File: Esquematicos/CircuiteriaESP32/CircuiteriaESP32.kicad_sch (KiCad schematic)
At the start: 8 parts, among them J1 Conn_01x19, J2 Conn_01x19

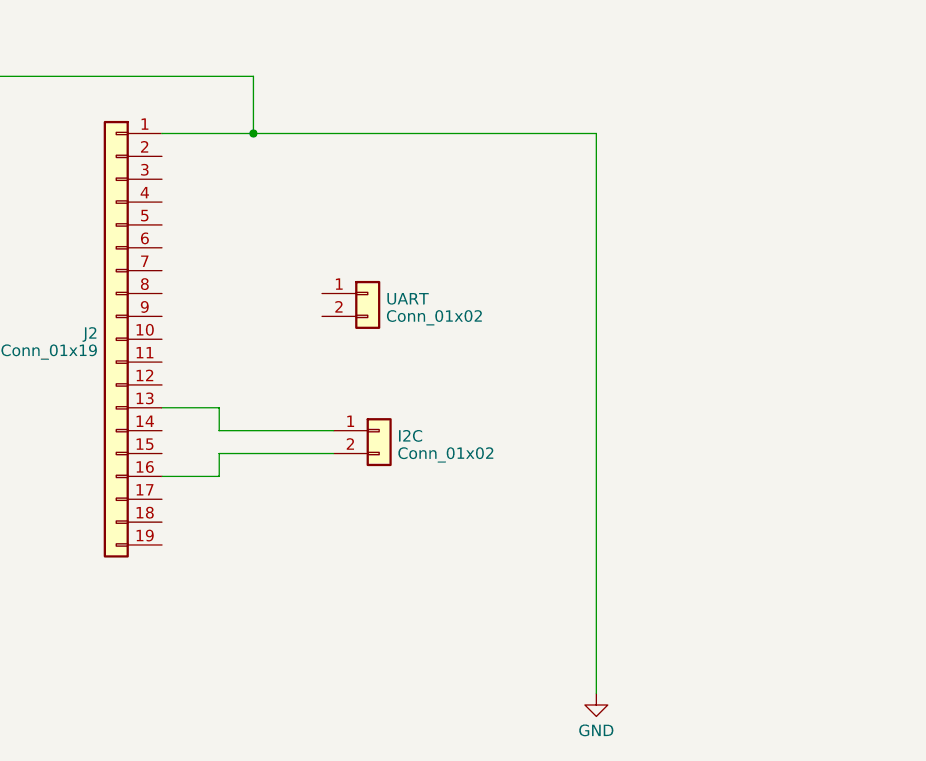
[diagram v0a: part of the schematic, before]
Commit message: Mejoras en el disenio kicad y más código generado
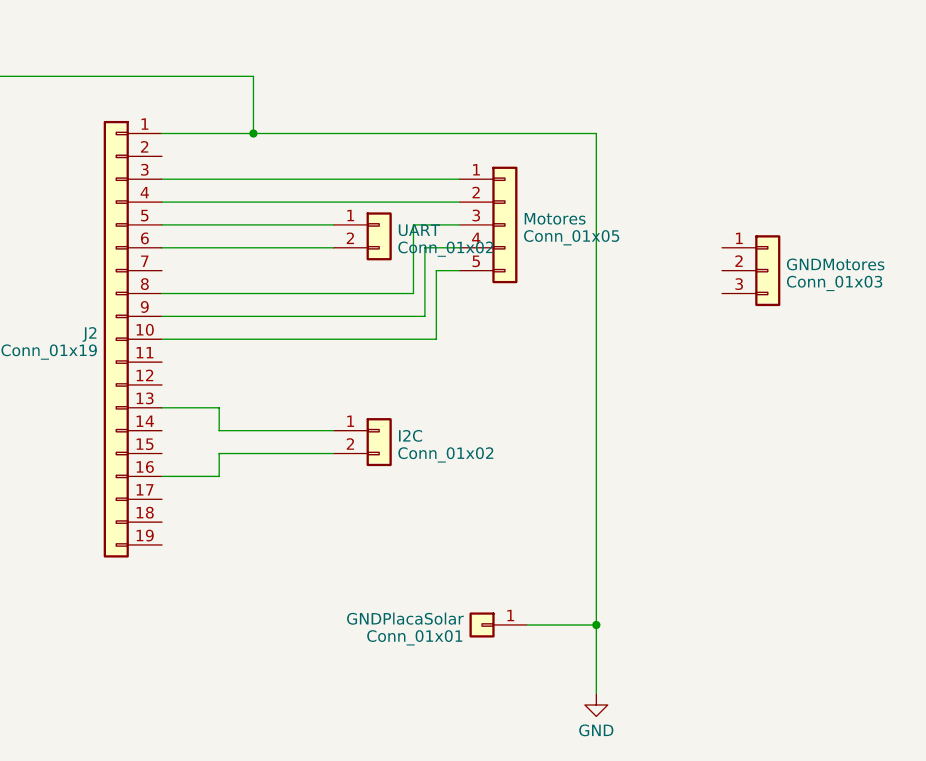
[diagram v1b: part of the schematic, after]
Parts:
- added GNDMotores: Conn_01x03, symbol Connector_Generic:Conn_01x03
- added GNDPlacaSolar: Conn_01x01, symbol Connector_Generic:Conn_01x01
- added Motores: Conn_01x05, symbol Connector_Generic:Conn_01x05
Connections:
- net GND: now also GNDPlacaSolar.1 (Pin_1)
- net at J2.10 (Pin_10): now also Motores.5 (Pin_5)
- net at J2.3 (Pin_3): now also Motores.1 (Pin_1)
- net at J2.4 (Pin_4): now also Motores.2 (Pin_2)
- net at J2.5 (Pin_5): now also UART.1 (Pin_1)
- net at J2.6 (Pin_6): now also UART.2 (Pin_2)
- net at J2.8 (Pin_8): now also Motores.3 (Pin_3)
- net at J2.9 (Pin_9): now also Motores.4 (Pin_4)
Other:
- moved on the sheet: UART
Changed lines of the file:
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@@
   (junction (at 86.36 45.72) (diameter 0) (color 0 0 0 0)
   )
+  (junction (at 184.15 100.33) (diameter 0) (color 0 0 0 0)
+  )
   (junction (at 64.77 45.72) (diameter 0) (color 0 0 0 0)
   )
@@
   (junction (at 90.17 63.5) (diameter 0) (color 0 0 0 0)
   )
+  (wire (pts (xy 168.91 60.96) (xy 166.37 60.96))
+    (stroke (width 0) (type default))
+  )
   (wire (pts (xy 64.77 91.44) (xy 64.77 76.2))
     (stroke (width 0) (type default))
@@
     (stroke (width 0) (type default))
   )
+  (wire (pts (xy 135.89 58.42) (xy 154.94 58.42))
+    (stroke (width 0) (type default))
+  )
   (wire (pts (xy 101.6 39.37) (xy 86.36 39.37))
     (stroke (width 0) (type default))
   )
+  (wire (pts (xy 163.83 63.5) (xy 135.89 63.5))
+    (stroke (width 0) (type default))
+  )
   (wire (pts (xy 64.77 76.2) (xy 69.85 76.2))
     (stroke (width 0) (type default))
   )
+  (wire (pts (xy 168.91 55.88) (xy 163.83 55.88))
+    (stroke (width 0) (type default))
+  )
+  (wire (pts (xy 176.53 100.33) (xy 184.15 100.33))
+    (stroke (width 0) (type default))
+  )
+  (wire (pts (xy 135.89 50.8) (xy 168.91 50.8))
+    (stroke (width 0) (type default))
+  )
   (wire (pts (xy 90.17 63.5) (xy 88.9 63.5))
     (stroke (width 0) (type default))
@@
     (stroke (width 0) (type default))
   )
+  (wire (pts (xy 168.91 58.42) (xy 165.1 58.42))
+    (stroke (width 0) (type default))
+  )
   (wire (pts (xy 135.89 45.72) (xy 146.05 45.72))
     (stroke (width 0) (type default))
@@
     (stroke (width 0) (type default))
   )
+  (wire (pts (xy 165.1 58.42) (xy 165.1 66.04))
+    (stroke (width 0) (type default))
+  )
   (wire (pts (xy 92.71 91.44) (xy 64.77 91.44))
     (stroke (width 0) (type default))
@@
     (stroke (width 0) (type default))
   )
-  (wire (pts (xy 184.15 45.72) (xy 184.15 107.95))
+  (wire (pts (xy 184.15 45.72) (xy 184.15 100.33))
+    (stroke (width 0) (type default))
+  )
+  (wire (pts (xy 166.37 60.96) (xy 166.37 68.58))
     (stroke (width 0) (type default))
   )
@@
     (stroke (width 0) (type default))
   )
+  (wire (pts (xy 166.37 68.58) (xy 135.89 68.58))
+    (stroke (width 0) (type default))
+  )
+  (wire (pts (xy 135.89 55.88) (xy 154.94 55.88))
+    (stroke (width 0) (type default))
+  )
   (wire (pts (xy 154.94 81.28) (xy 142.24 81.28))
     (stroke (width 0) (type default))
@@
   )
   (wire (pts (xy 88.9 58.42) (xy 92.71 58.42))
+    (stroke (width 0) (type default))
+  )
+  (wire (pts (xy 135.89 53.34) (xy 168.91 53.34))
+    (stroke (width 0) (type default))
+  )
+  (wire (pts (xy 165.1 66.04) (xy 135.89 66.04))
+    (stroke (width 0) (type default))
+  )
+  (wire (pts (xy 184.15 100.33) (xy 184.15 107.95))
+    (stroke (width 0) (type default))
+  )
+  (wire (pts (xy 163.83 55.88) (xy 163.83 63.5))
     (stroke (width 0) (type default))
   )
@@
     )
   )
+  (symbol (lib_id "Connector_Generic:Conn_01x03") (at 203.2 60.96 0) (unit 1)
+    (in_bom yes) (on_board yes) (dnp no) (fields_autoplaced)
+    (property "Reference" "GNDMotores" (at 205.232 60.3163 0)
+      (effects (font (size 1.27 1.27)) (justify left))
+    )
+    (property "Value" "Conn_01x03" (at 205.232 62.2373 0)
+      (effects (font (size 1.27 1.27)) (justify left))
+    )
+    (property "Footprint" "" (at 203.2 60.96 0)
+      (effects (font (size 1.27 1.27)) hide)
+    )
+    (property "Datasheet" "~" (at 203.2 60.96 0)
+      (effects (font (size 1.27 1.27)) hide)
+    )
+    (pin "1")
+    (pin "2")
+    (pin "3")
+    (instances
+      (project "CircuiteriaESP32"
+        (path "/916eeabf-7d1d-4f94-90a9-b50ef7656e3c"
+          (reference "GNDMotores") (unit 1)
+        )
+      )
+    )
+  )
   (symbol (lib_id "Device:C_Polarized_US") (at 105.41 39.37 90) (unit 1)
     (in_bom yes) (on_board yes) (dnp no) (fields_autoplaced)
@@
         (path "/916eeabf-7d1d-4f94-90a9-b50ef7656e3c"
           (reference "C1") (unit 1)
+        )
+      )
+    )
+  )
+  (symbol (lib_id "Connector_Generic:Conn_01x05") (at 173.99 55.88 0) (unit 1)
+    (in_bom yes) (on_board yes) (dnp no) (fields_autoplaced)
+    (property "Reference" "Motores" (at 176.022 55.2363 0)
+      (effects (font (size 1.27 1.27)) (justify left))
+    )
+    (property "Value" "Conn_01x05" (at 176.022 57.1573 0)
+      (effects (font (size 1.27 1.27)) (justify left))
+    )
+    (property "Footprint" "" (at 173.99 55.88 0)
+      (effects (font (size 1.27 1.27)) hide)
+    )
+    (property "Datasheet" "~" (at 173.99 55.88 0)
+      (effects (font (size 1.27 1.27)) hide)
+    )
+    (pin "1")
+    (pin "2")
+    (pin "3")
+    (pin "4")
+    (pin "5")
+    (instances
+      (project "CircuiteriaESP32"
+        (path "/916eeabf-7d1d-4f94-90a9-b50ef7656e3c"
+          (reference "Motores") (unit 1)
         )
       )
@@
     )
   )
-  (symbol (lib_id "Connector_Generic:Conn_01x02") (at 158.75 63.5 0) (unit 1)
-    (in_bom yes) (on_board yes) (dnp no) (fields_autoplaced)
-    (property "Reference" "UART" (at 160.782 64.1263 0)
-      (effects (font (size 1.27 1.27)) (justify left))
-    )
-    (property "Value" "Conn_01x02" (at 160.782 66.0473 0)
-      (effects (font (size 1.27 1.27)) (justify left))
-    )
-    (property "Footprint" "" (at 158.75 63.5 0)
-      (effects (font (size 1.27 1.27)) hide)
-    )
-    (property "Datasheet" "~" (at 158.75 63.5 0)
+  (symbol (lib_id "Connector_Generic:Conn_01x02") (at 160.02 55.88 0) (unit 1)
+    (in_bom yes) (on_board yes) (dnp no) (fields_autoplaced)
+    (property "Reference" "UART" (at 162.052 56.5063 0)
+      (effects (font (size 1.27 1.27)) (justify left))
+    )
+    (property "Value" "Conn_01x02" (at 162.052 58.4273 0)
+      (effects (font (size 1.27 1.27)) (justify left))
+    )
+    (property "Footprint" "" (at 160.02 55.88 0)
+      (effects (font (size 1.27 1.27)) hide)
+    )
+    (property "Datasheet" "~" (at 160.02 55.88 0)
       (effects (font (size 1.27 1.27)) hide)
     )
@@
         )
       )
+    )
+  )
+  (symbol (lib_id "Connector_Generic:Conn_01x01") (at 171.45 100.33 0) (mirror y) (unit 1)
+    (in_bom yes) (on_board yes) (dnp no)
+    (property "Reference" "GNDPlacaSolar" (at 169.418 99.6863 0)
+      (effects (font (size 1.27 1.27)) (justify left))
+    )
+    (property "Value" "Conn_01x01" (at 169.418 101.6073 0)
+      (effects (font (size 1.27 1.27)) (justify left))
+    )
+    (property "Footprint" "" (at 171.45 100.33 0)
+      (effects (font (size 1.27 1.27)) hide)
+    )
+    (property "Datasheet" "~" (at 171.45 100.33 0)
+      (effects (font (size 1.27 1.27)) hide)
+    )
+    (pin "1")
+    (instances
+      (project "CircuiteriaESP32"
+        (path "/916eeabf-7d1d-4f94-90a9-b50ef7656e3c"
+          (reference "GNDPlacaSolar") (unit 1)
+        )
+      )

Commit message: Ajustadas algunas cosas, to-do
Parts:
- added GPSRX: Conn_01x01, symbol Connector_Generic:Conn_01x01
- added R1, R2: 4k7, symbol Device:R
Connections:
- net +5V: now also R1.2, R2.2
- net at I2C.1 (Pin_1), J2.13 (Pin_13): now also R2.1
- net at I2C.2 (Pin_2), J2.16 (Pin_16): now also R1.1
- net at Motores.1 (Pin_1): now also J2.2 (Pin_2); no longer J2.3 (Pin_3)
- net at Motores.2 (Pin_2): now also J2.3 (Pin_3); no longer J2.4 (Pin_4)
- net at Motores.3 (Pin_3): now also J2.6 (Pin_6); no longer J2.8 (Pin_8)
- net at Motores.4 (Pin_4): now also J2.8 (Pin_8); no longer J2.9 (Pin_9)
- net at J2.10 (Pin_10): now also GPSRX.1 (Pin_1); no longer Motores.5 (Pin_5)
- net at UART.1 (Pin_1): now also J2.4 (Pin_4); no longer J2.5 (Pin_5)
- net at UART.2 (Pin_2): now also J2.5 (Pin_5); no longer J2.6 (Pin_6)
- new net: J2.9 (Pin_9), Motores.5 (Pin_5)
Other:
- moved on the sheet: UART
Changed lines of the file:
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@@
 (kicad_sch (version 20230121) (generator eeschema)
   (paper "A4")
+  (junction (at 146.05 97.79) (diameter 0) (color 0 0 0 0)
+  )
+  (junction (at 146.05 81.28) (diameter 0) (color 0 0 0 0)
+  )
   (junction (at 64.77 76.2) (diameter 0) (color 0 0 0 0)
   )
   (junction (at 86.36 45.72) (diameter 0) (color 0 0 0 0)
   )
+  (junction (at 153.67 78.74) (diameter 0) (color 0 0 0 0)
+  )
   (junction (at 184.15 100.33) (diameter 0) (color 0 0 0 0)
   )
@@
   (junction (at 90.17 63.5) (diameter 0) (color 0 0 0 0)
   )
-  (wire (pts (xy 168.91 60.96) (xy 166.37 60.96))
-    (stroke (width 0) (type default))
+  (junction (at 64.77 91.44) (diameter 0) (color 0 0 0 0)
   )
   (wire (pts (xy 64.77 91.44) (xy 64.77 76.2))
@@
     (stroke (width 0) (type default))
   )
-  (wire (pts (xy 135.89 58.42) (xy 154.94 58.42))
+  (wire (pts (xy 165.1 58.42) (xy 165.1 63.5))
+    (stroke (width 0) (type default))
+  )
+  (wire (pts (xy 153.67 78.74) (xy 142.24 78.74))
+    (stroke (width 0) (type default))
+  )
+  (wire (pts (xy 146.05 92.71) (xy 146.05 97.79))
     (stroke (width 0) (type default))
   )
@@
     (stroke (width 0) (type default))
   )
-  (wire (pts (xy 163.83 63.5) (xy 135.89 63.5))
-    (stroke (width 0) (type default))
-  )
   (wire (pts (xy 64.77 76.2) (xy 69.85 76.2))
     (stroke (width 0) (type default))
   )
-  (wire (pts (xy 168.91 55.88) (xy 163.83 55.88))
+  (wire (pts (xy 135.89 66.04) (xy 167.64 66.04))
     (stroke (width 0) (type default))
   )
@@
     (stroke (width 0) (type default))
   )
-  (wire (pts (xy 135.89 50.8) (xy 168.91 50.8))
-    (stroke (width 0) (type default))
-  )
   (wire (pts (xy 90.17 63.5) (xy 88.9 63.5))
     (stroke (width 0) (type default))
   )
+  (wire (pts (xy 135.89 55.88) (xy 154.94 55.88))
+    (stroke (width 0) (type default))
+  )
+  (wire (pts (xy 176.53 74.93) (xy 153.67 74.93))
+    (stroke (width 0) (type default))
+  )
   (wire (pts (xy 86.36 45.72) (xy 92.71 45.72))
     (stroke (width 0) (type default))
@@
     (stroke (width 0) (type default))
   )
+  (wire (pts (xy 162.56 58.42) (xy 135.89 58.42))
+    (stroke (width 0) (type default))
+  )
+  (wire (pts (xy 168.91 58.42) (xy 165.1 58.42))
+    (stroke (width 0) (type default))
+  )
+  (wire (pts (xy 153.67 85.09) (xy 176.53 85.09))
+    (stroke (width 0) (type default))
+  )
   (wire (pts (xy 64.77 76.2) (xy 64.77 45.72))
     (stroke (width 0) (type default))
   )
-  (wire (pts (xy 168.91 58.42) (xy 165.1 58.42))
-    (stroke (width 0) (type default))
-  )
   (wire (pts (xy 135.89 45.72) (xy 146.05 45.72))
     (stroke (width 0) (type default))
@@
     (stroke (width 0) (type default))
   )
+  (wire (pts (xy 168.91 53.34) (xy 166.37 53.34))
+    (stroke (width 0) (type default))
+  )
   (wire (pts (xy 88.9 63.5) (xy 88.9 64.77))
     (stroke (width 0) (type default))
   )
-  (wire (pts (xy 165.1 58.42) (xy 165.1 66.04))
+  (wire (pts (xy 135.89 53.34) (xy 154.94 53.34))
+    (stroke (width 0) (type default))
+  )
+  (wire (pts (xy 176.53 85.09) (xy 176.53 74.93))
     (stroke (width 0) (type default))
   )
@@
     (stroke (width 0) (type default))
   )
-  (wire (pts (xy 166.37 60.96) (xy 166.37 68.58))
+  (wire (pts (xy 168.91 50.8) (xy 167.64 50.8))
     (stroke (width 0) (type default))
   )
@@
     (stroke (width 0) (type default))
   )
-  (wire (pts (xy 166.37 68.58) (xy 135.89 68.58))
-    (stroke (width 0) (type default))
-  )
-  (wire (pts (xy 135.89 55.88) (xy 154.94 55.88))
-    (stroke (width 0) (type default))
-  )
-  (wire (pts (xy 154.94 81.28) (xy 142.24 81.28))
+  (wire (pts (xy 154.94 81.28) (xy 146.05 81.28))
     (stroke (width 0) (type default))
   )
@@
     (stroke (width 0) (type default))
   )
+  (wire (pts (xy 167.64 60.96) (xy 167.64 66.04))
+    (stroke (width 0) (type default))
+  )
+  (wire (pts (xy 146.05 97.79) (xy 64.77 97.79))
+    (stroke (width 0) (type default))
+  )
   (wire (pts (xy 90.17 76.2) (xy 90.17 63.5))
     (stroke (width 0) (type default))
   )
-  (wire (pts (xy 154.94 78.74) (xy 142.24 78.74))
+  (wire (pts (xy 154.94 78.74) (xy 153.67 78.74))
     (stroke (width 0) (type default))
   )
@@
     (stroke (width 0) (type default))
   )
+  (wire (pts (xy 167.64 50.8) (xy 167.64 48.26))
+    (stroke (width 0) (type default))
+  )
+  (wire (pts (xy 162.56 55.88) (xy 162.56 58.42))
+    (stroke (width 0) (type default))
+  )
   (wire (pts (xy 64.77 41.91) (xy 64.77 45.72))
     (stroke (width 0) (type default))
   )
+  (wire (pts (xy 146.05 81.28) (xy 146.05 85.09))
+    (stroke (width 0) (type default))
+  )
   (wire (pts (xy 146.05 39.37) (xy 146.05 45.72))
     (stroke (width 0) (type default))
   )
+  (wire (pts (xy 146.05 81.28) (xy 142.24 81.28))
+    (stroke (width 0) (type default))
+  )
+  (wire (pts (xy 153.67 74.93) (xy 153.67 78.74))
+    (stroke (width 0) (type default))
+  )
+  (wire (pts (xy 168.91 60.96) (xy 167.64 60.96))
+    (stroke (width 0) (type default))
+  )
+  (wire (pts (xy 153.67 92.71) (xy 153.67 97.79))
+    (stroke (width 0) (type default))
+  )
   (wire (pts (xy 146.05 45.72) (xy 184.15 45.72))
     (stroke (width 0) (type default))
@@
     (stroke (width 0) (type default))
   )
-  (wire (pts (xy 135.89 53.34) (xy 168.91 53.34))
-    (stroke (width 0) (type default))
-  )
-  (wire (pts (xy 165.1 66.04) (xy 135.89 66.04))
+  (wire (pts (xy 153.67 97.79) (xy 146.05 97.79))
+    (stroke (width 0) (type default))
+  )
+  (wire (pts (xy 166.37 53.34) (xy 166.37 50.8))
+    (stroke (width 0) (type default))
+  )
+  (wire (pts (xy 167.64 48.26) (xy 135.89 48.26))
     (stroke (width 0) (type default))
   )
@@
     (stroke (width 0) (type default))
   )
-  (wire (pts (xy 163.83 55.88) (xy 163.83 63.5))
+  (wire (pts (xy 166.37 50.8) (xy 135.89 50.8))
+    (stroke (width 0) (type default))
+  )
+  (wire (pts (xy 168.91 55.88) (xy 162.56 55.88))
     (stroke (width 0) (type default))
   )
@@
   )
   (wire (pts (xy 86.36 39.37) (xy 86.36 45.72))
+    (stroke (width 0) (type default))
+  )
+  (wire (pts (xy 64.77 97.79) (xy 64.77 91.44))
+    (stroke (width 0) (type default))
+  )
+  (wire (pts (xy 135.89 68.58) (xy 161.29 68.58))
+    (stroke (width 0) (type default))
+  )
+  (wire (pts (xy 165.1 63.5) (xy 135.89 63.5))
     (stroke (width 0) (type default))
   )
@@
     )
   )
+  (symbol (lib_id "Connector_Generic:Conn_01x01") (at 166.37 68.58 0) (unit 1)
+    (in_bom yes) (on_board yes) (dnp no)
+    (property "Reference" "GPSRX" (at 168.402 67.9363 0)
+      (effects (font (size 1.27 1.27)) (justify left))
+    )
+    (property "Value" "Conn_01x01" (at 168.402 69.8573 0)
+      (effects (font (size 1.27 1.27)) (justify left))
+    )
+    (property "Footprint" "" (at 166.37 68.58 0)
+      (effects (font (size 1.27 1.27)) hide)
+    )
+    (property "Datasheet" "~" (at 166.37 68.58 0)
+      (effects (font (size 1.27 1.27)) hide)
+    )
+    (pin "1")
+    (instances
+      (project "CircuiteriaESP32"
+        (path "/916eeabf-7d1d-4f94-90a9-b50ef7656e3c"
+          (reference "GPSRX") (unit 1)
+        )
+      )
+    )
+  )
   (symbol (lib_id "Device:D") (at 73.66 76.2 0) (unit 1)
     (in_bom yes) (on_board yes) (dnp no) (fields_autoplaced)
@@
         (path "/916eeabf-7d1d-4f94-90a9-b50ef7656e3c"
           (reference "#PWR02") (unit 1)
+        )
+      )
+    )
+  )
+  (symbol (lib_id "Device:R") (at 146.05 88.9 0) (unit 1)
+    (in_bom yes) (on_board yes) (dnp no) (fields_autoplaced)
+    (property "Reference" "R1" (at 147.828 88.2563 0)
+      (effects (font (size 1.27 1.27)) (justify left))
+    )
+    (property "Value" "4k7" (at 147.828 90.1773 0)
+      (effects (font (size 1.27 1.27)) (justify left))
+    )
+    (property "Footprint" "" (at 144.272 88.9 90)
+      (effects (font (size 1.27 1.27)) hide)
+    )
+    (property "Datasheet" "~" (at 146.05 88.9 0)
+      (effects (font (size 1.27 1.27)) hide)
+    )
+    (pin "1")
+    (pin "2")
+    (instances
+      (project "CircuiteriaESP32"
+        (path "/916eeabf-7d1d-4f94-90a9-b50ef7656e3c"
+          (reference "R1") (unit 1)
         )
       )
@@
     )
   )
-  (symbol (lib_id "Connector_Generic:Conn_01x02") (at 160.02 55.88 0) (unit 1)
-    (in_bom yes) (on_board yes) (dnp no) (fields_autoplaced)
-    (property "Reference" "UART" (at 162.052 56.5063 0)
-      (effects (font (size 1.27 1.27)) (justify left))
-    )
-    (property "Value" "Conn_01x02" (at 162.052 58.4273 0)
-      (effects (font (size 1.27 1.27)) (justify left))
-    )
-    (property "Footprint" "" (at 160.02 55.88 0)
-      (effects (font (size 1.27 1.27)) hide)
-    )
-    (property "Datasheet" "~" (at 160.02 55.88 0)
+  (symbol (lib_id "Connector_Generic:Conn_01x02") (at 160.02 53.34 0) (unit 1)
+    (in_bom yes) (on_board yes) (dnp no) (fields_autoplaced)
+    (property "Reference" "UART" (at 162.052 53.9663 0)
+      (effects (font (size 1.27 1.27)) (justify left))
+    )
+    (property "Value" "Conn_01x02" (at 162.052 55.8873 0)
+      (effects (font (size 1.27 1.27)) (justify left))
+    )
+    (property "Footprint" "" (at 160.02 53.34 0)
+      (effects (font (size 1.27 1.27)) hide)
+    )
+    (property "Datasheet" "~" (at 160.02 53.34 0)
       (effects (font (size 1.27 1.27)) hide)
     )
@@
         )
       )
+    )
+  )
+  (symbol (lib_id "Device:R") (at 153.67 88.9 0) (unit 1)
+    (in_bom yes) (on_board yes) (dnp no) (fields_autoplaced)
+    (property "Reference" "R2" (at 155.448 88.2563 0)
+      (effects (font (size 1.27 1.27)) (justify left))
+    )
+    (property "Value" "4k7" (at 155.448 90.1773 0)
+      (effects (font (size 1.27 1.27)) (justify left))
+    )
+    (property "Footprint" "" (at 151.892 88.9 90)
+      (effects (font (size 1.27 1.27)) hide)
+    )
+    (property "Datasheet" "~" (at 153.67 88.9 0)
+      (effects (font (size 1.27 1.27)) hide)
+    )
+    (pin "1")
+    (pin "2")
+    (instances
+      (project "CircuiteriaESP32"
+        (path "/916eeabf-7d1d-4f94-90a9-b50ef7656e3c"
+          (reference "R2") (unit 1)
+        )
+      )
